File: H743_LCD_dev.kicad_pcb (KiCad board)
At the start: 6 copper layers, 80 x 65 mm, 76 parts, among them J1 Micro_SD_Card_Det_Hirose_DM3AT, J2 TFT_LCD, J3 CAPACITIVE_CONTROLLER, J4 USB-C, J5 I2C-STEMMA-QT, J7 Conn_02x05_Odd_Even, J8 SPKR, J9 UART, U1 W25Q128JVS, U2 IS42S16160J-7TL, U3 MT9284, U4 STM32H723ZGTx, U5 W25N01GVZEIG, U6 MAX98357AETE_, U7 CAT24C128, Y1 25MHz, Y2 32.768KHz

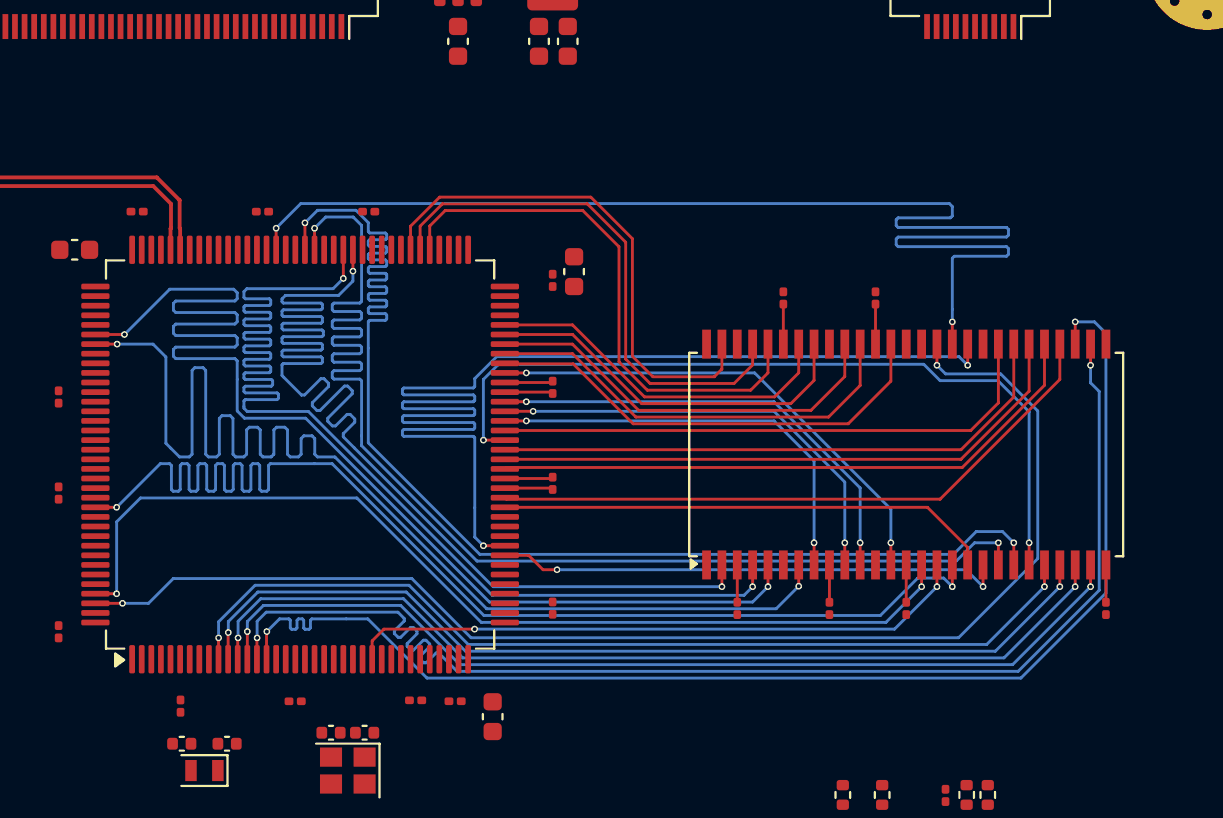
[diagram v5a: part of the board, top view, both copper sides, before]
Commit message: Finish high speed sdram tracks
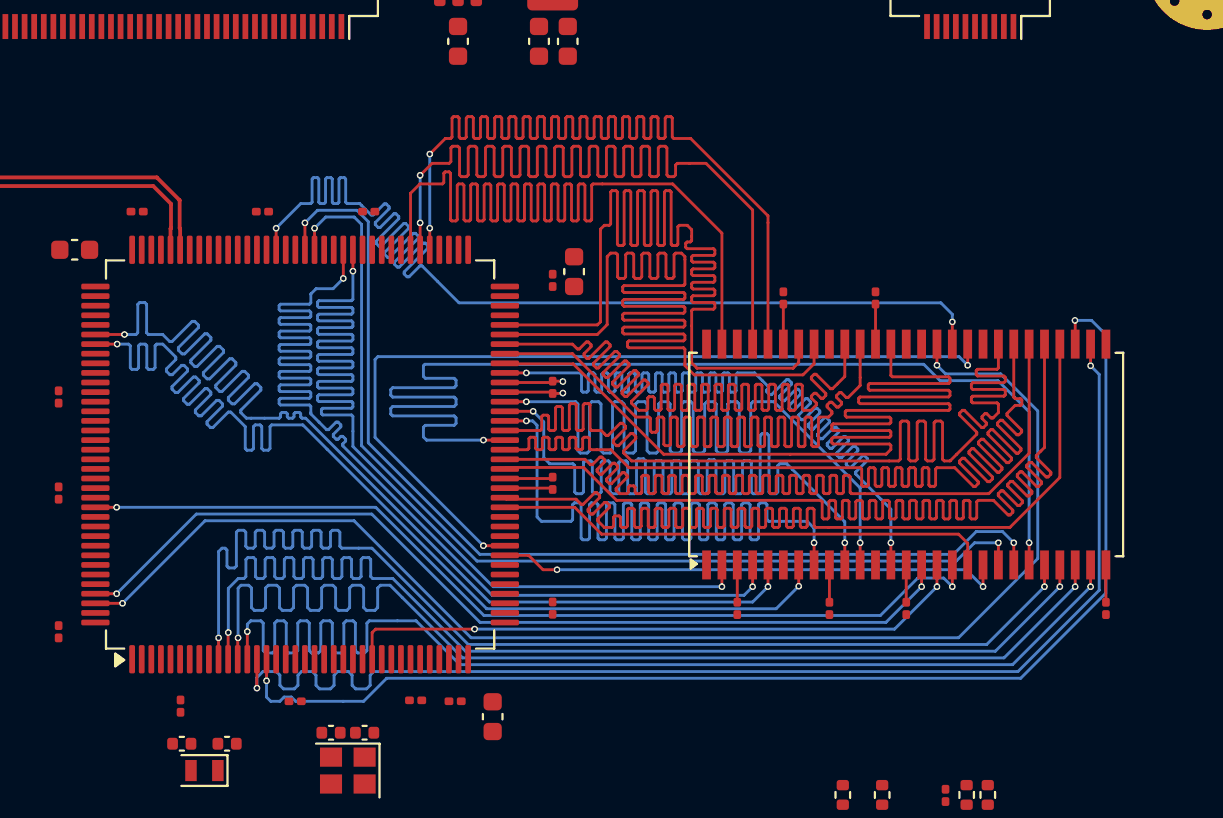
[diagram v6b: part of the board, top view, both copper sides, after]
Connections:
- net /MCU/A0 renamed /MCU/SDRAM_ADD0
- net /MCU/A1 renamed /MCU/SDRAM_ADD1
- net /MCU/A10 renamed /MCU/SDRAM_ADD10
- net /MCU/A11 renamed /MCU/SDRAM_ADD11
- net /MCU/A2 renamed /MCU/SDRAM_ADD2
- net /MCU/A3 renamed /MCU/SDRAM_ADD3
- net /MCU/A4 renamed /MCU/SDRAM_ADD4
- net /MCU/A5 renamed /MCU/SDRAM_ADD5
- net /MCU/A6 renamed /MCU/SDRAM_ADD6
- net /MCU/A7 renamed /MCU/SDRAM_ADD7
- net /MCU/A8 renamed /MCU/SDRAM_ADD8
- net /MCU/A9 renamed /MCU/SDRAM_ADD9
- net /MCU/DQ0 renamed /MCU/SDRAM_DQ0
- net /MCU/DQ1 renamed /MCU/SDRAM_DQ1
- net /MCU/DQ10 renamed /MCU/SDRAM_DQ10
- net /MCU/DQ11 renamed /MCU/SDRAM_DQ11
- net /MCU/DQ12 renamed /MCU/SDRAM_DQ12
- net /MCU/DQ13 renamed /MCU/SDRAM_DQ13
- net /MCU/DQ14 renamed /MCU/SDRAM_DQ14
- net /MCU/DQ15 renamed /MCU/SDRAM_DQ15
- net /MCU/DQ2 renamed /MCU/SDRAM_DQ2
- net /MCU/DQ3 renamed /MCU/SDRAM_DQ3
- net /MCU/DQ4 renamed /MCU/SDRAM_DQ4
- net /MCU/DQ5 renamed /MCU/SDRAM_DQ5
- net /MCU/DQ6 renamed /MCU/SDRAM_DQ6
- net /MCU/DQ7 renamed /MCU/SDRAM_DQ7
- net /MCU/DQ8 renamed /MCU/SDRAM_DQ8
- net /MCU/DQ9 renamed /MCU/SDRAM_DQ9
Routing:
- net /MCU/SDRAM_DQ12: track 18.9 -> 68.0 mm
- net /MCU/SDRAM_DQ11: track 20.0 -> 68.0 mm
- net /MCU/SDRAM_DQ10: track 21.5 -> 68.0 mm
- net /MCU/SDRAM_DQ8: track 24.3 -> 68.0 mm
- net /MCU/SDRAM_DQ4: track 22.4 -> 64.9 mm
- net /MCU/SDRAM_DQ5: track 23.5 -> 64.9 mm
- net /MCU/SDRAM_DQ15: track 27.0 -> 68.0 mm
- net /MCU/SDRAM_DQ6: track 24.4 -> 64.9 mm
- net /MCU/SDRAM_DQ14: track 28.0 -> 67.9 mm, vias 0 -> 2
- net /MCU/SDRAM_DQ7: track 25.9 -> 64.9 mm
- net /MCU/SDRAM_ADD11: track 29.4 -> 68.0 mm
- net /MCU/SDRAM_DQ9: track 22.7 -> 60.7 mm
- net /MCU/SDRAM_ADD9: track 30.4 -> 68.0 mm
- net /MCU/SDRAM_ADD8: track 31.2 -> 68.0 mm
- net /MCU/SDRAM_DQ13: track 28.4 -> 64.9 mm, vias 0 -> 2
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
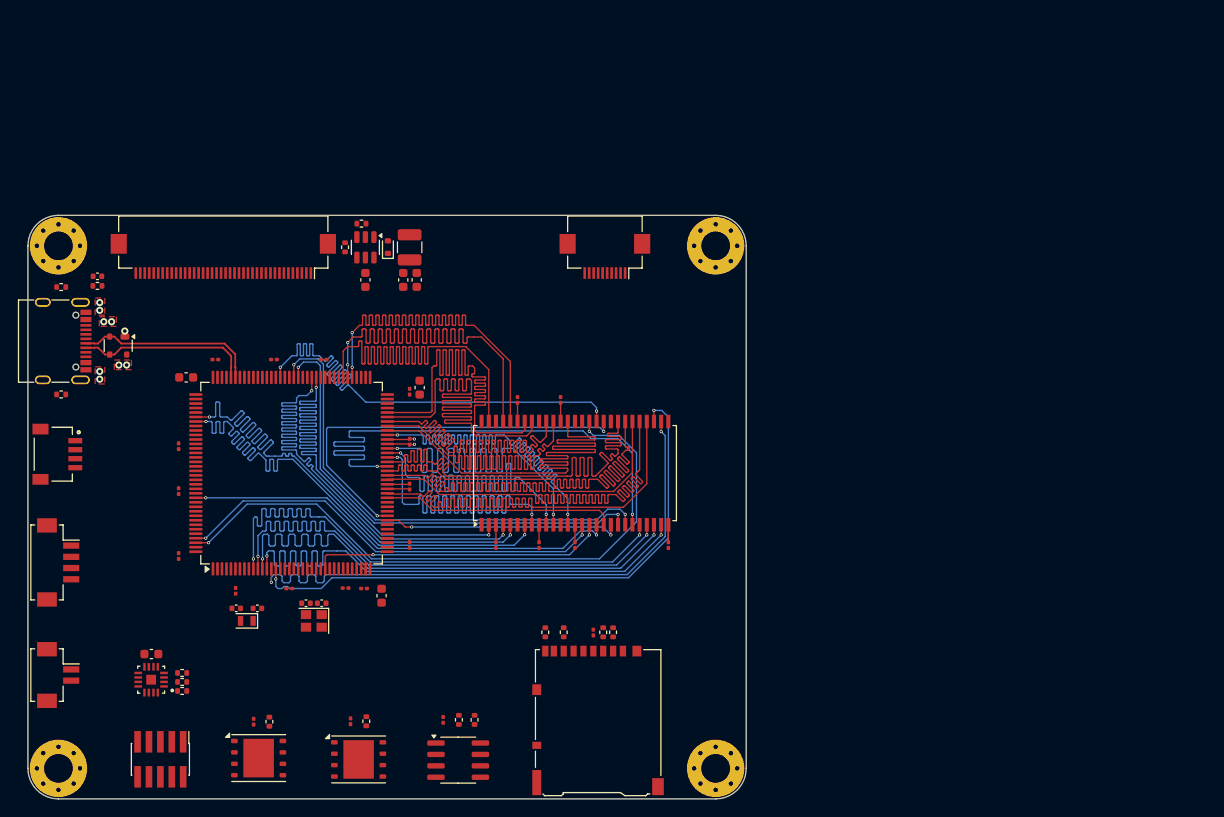
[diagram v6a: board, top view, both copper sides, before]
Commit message: Finish sdram, LCD, SD-card, QSPI, I2S tracks
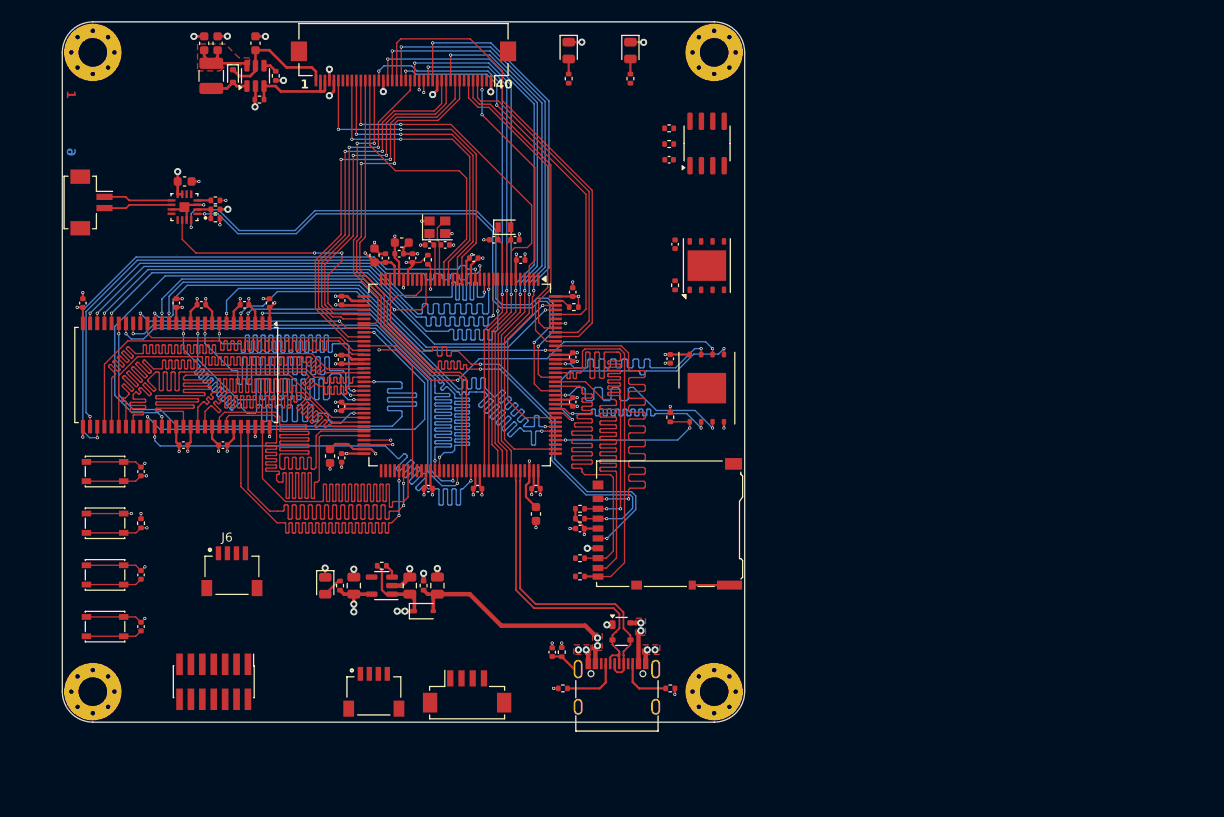
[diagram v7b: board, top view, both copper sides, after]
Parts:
- removed J7: Conn_02x05_Odd_Even, Connector_PinHeader_1.27mm:PinHeader_2x05_P1.27mm_Vertical_SMD
- added C24: 100n, Capacitor_SMD:C_0402_1005Metric, F.Cu at (115.0, 98.4)
- added C25: 100n, Capacitor_SMD:C_0402_1005Metric, F.Cu at (143.7, 74.2)
- added C26: 1u, Capacitor_SMD:C_0603_1608Metric, F.Cu at (144.0, 72.9)
- added C27: 100n, Capacitor_SMD:C_0402_1005Metric, F.Cu at (115.0, 109.9)
- added C28: 100n, Capacitor_SMD:C_0402_1005Metric, F.Cu at (115.0, 115.7)
- added C29: 100n, Capacitor_SMD:C_0402_1005Metric, F.Cu at (129.3, 79.7)
- added C30: 1u, Capacitor_SMD:C_0805_2012Metric, F.Cu at (144.9, 111.1)
- added C44: 2.2u, Capacitor_SMD:C_0805_2012Metric, F.Cu at (138.7, 111.1)
- added C45: 10u, Capacitor_SMD:C_0805_2012Metric, F.Cu at (148.0, 111.1)
- added D3: NSR0340HT1G, Diode_SMD:D_SOD-323, F.Cu at (146.5, 114.0)
- added D4: LED, LED_SMD:LED_0805_2012Metric, F.Cu at (135.5, 111.2)
- added D5: LED, LED_SMD:LED_0805_2012Metric, F.Cu at (169.5, 51.5)
- added D6: LED, LED_SMD:LED_0805_2012Metric, F.Cu at (162.6, 51.5)
- added J6: UART, SM04B-SRSS-TB_LF__SN_:JST_SM04B-SRSS-TB_LF__SN_, F.Cu at (125.1, 107.5)
- added R17: 10K, Resistor_SMD:R_0402_1005Metric, F.Cu at (146.9, 74.8)
- added R18: 10K, Resistor_SMD:R_0402_1005Metric, F.Cu at (115.0, 104.2)
- added R19: 10K, Resistor_SMD:R_0402_1005Metric, F.Cu at (163.2, 80.1)
- added R20: 10K, Resistor_SMD:R_0402_1005Metric, F.Cu at (141.8, 108.9)
- added R21: 2K2, Resistor_SMD:R_0402_1005Metric, F.Cu at (137.1, 111.1)
- added R22: 100K, Resistor_SMD:R_0402_1005Metric, F.Cu at (146.4, 111.1)
- added R23: 1K, Resistor_SMD:R_0402_1005Metric, F.Cu at (169.5, 54.7)
- added R24: 1K, Resistor_SMD:R_0402_1005Metric, F.Cu at (162.6, 54.7)
- added SW1: SW_Push, Button_Switch_SMD:SW_SPST_PTS810, F.Cu at (111.0, 98.4)
- added SW2: SW_Push, Button_Switch_SMD:SW_SPST_PTS810, F.Cu at (111.0, 104.2)
- added SW3: SW_Push, Button_Switch_SMD:SW_SPST_PTS810, F.Cu at (111.0, 109.9)
- added SW4: SW_Push, Button_Switch_SMD:SW_SPST_PTS810, F.Cu at (111.0, 115.7)
- added U8: TLV75733PDBV, Package_TO_SOT_SMD:SOT-23-5, F.Cu at (141.8, 111.1)
- C1, C10, C11, C12, C13, C14, C15, C16, C17, C18, C2, C20, C21, C22, C3, C36, C37, C38, C4, C5, C6, C7, C8, C9: footprint Capacitor_SMD:C_0201_0603Metric -> Capacitor_SMD:C_0402_1005Metric
- J3: value CAPACITIVE_CONTROLLER -> swd; footprint Connector_FFC-FPC:Hirose_FH12-10S-0.5SH_1x10-1MP_P0.50mm_Horizontal -> Connector_PinHeader_1.27mm:PinHeader_2x07_P1.27mm_Vertical_SMD
- U1: footprint Package_SON:WSON-8-1EP_6x5mm_P1.27mm_EP3.4x4.3mm -> Package_SON:WSON-8-1EP_8x6mm_P1.27mm_EP3.4x4.3mm
- moved H2 108.1 mm to (178.8, 51.7), turned to 180 degrees
- moved H1 105.7 mm to (109.6, 51.7), turned to 180 degrees
- moved H3 88.3 mm to (178.8, 122.9), turned to 180 degrees
- moved H4 85.3 mm to (109.6, 122.9), turned to 180 degrees
- moved R12 75.3 mm to (173.9, 122.6)
- moved J4 74.3 mm to (168.0, 123.6), turned to 0 degrees
- moved U7 74.1 mm to (178.0, 61.9), turned to 90 degrees
- moved R11 71.6 mm to (162.0, 122.6), turned to 0 degrees
- moved C1 70.6 mm to (108.5, 79.7), turned to 90 degrees
- moved R6 69.4 mm to (173.8, 60.2), turned to 180 degrees
- moved R5 68.3 mm to (173.8, 61.9), turned to 180 degrees
- moved U5 67.3 mm to (178.0, 75.5), turned to 90 degrees
- moved C20 67.3 mm to (173.8, 63.7), turned to 180 degrees
- moved R13 65.9 mm to (161.8, 118.5), turned to 90 degrees
- moved C43 65.7 mm to (160.8, 118.5), turned to 90 degrees
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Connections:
- C32 pad 1: Net-(U3-VIN) -> VDD
- C33 pad 1: Net-(U3-VIN) -> VDD
- J1 pad 1: /MEMORY/SD_DAT2 -> /MCU/SD_DAT2
- J1 pad 2: /MEMORY/SD_DAT3/CD -> /MCU/SD_DAT3
- J1 pad 3: /MEMORY/SD_CMD -> /MCU/SD_CMD
- J1 pad 5: /MEMORY/SD_CLK -> /MCU/SD_CLK
- J1 pad 7: /MEMORY/SD_DAT0 -> /MCU/SD_DAT0
- J1 pad 8: /MEMORY/SD_DAT1 -> /MCU/SD_DAT1
- J1 pad 9: /MEMORY/SD_DET -> /MCU/PG13
- J2 pad 1: /LCD/LED_K -> GND
- J2 pad 11: /LCD/LCD_R6 -> /LCD/LCD_R4
- J2 pad 12: /LCD/LCD_R7 -> /LCD/LCD_R3
- J2 pad 13: /LCD/LCD_G0 -> GND
- J2 pad 14: /LCD/LCD_G1 -> /LCD/LCD_G7
- J2 pad 15: /LCD/LCD_G2 -> /LCD/LCD_G6
- J2 pad 16: /LCD/LCD_G3 -> /LCD/LCD_G5
- J2 pad 18: /LCD/LCD_G5 -> /LCD/LCD_G3
- J2 pad 19: /LCD/LCD_G6 -> /LCD/LCD_G2
- J2 pad 2: /LCD/LED_A -> +3V3
- J2 pad 20: /LCD/LCD_G7 -> /LCD/LCD_B7
- J2 pad 21: /LCD/LCD_B0 -> /LCD/LCD_B6
- J2 pad 22: /LCD/LCD_B1 -> /LCD/LCD_B5
- J2 pad 23: /LCD/LCD_B2 -> /LCD/LCD_B4
- J2 pad 25: /LCD/LCD_B4 -> GND
- J2 pad 26: /LCD/LCD_B5 -> /LCD/HSYNC
- J2 pad 27: /LCD/LCD_B6 -> /LCD/VSYNC
- J2 pad 28: /LCD/LCD_B7 -> /LCD/LCD_DE
- J2 pad 29: GND -> /LCD/LCD_CLK
- J2 pad 3: unconnected-(J2-Pad3) -> /LCD/LCD_TP_RST
- J2 pad 30: /LCD/LCD_CLK -> /LCD/LCD_SPI_CS
- J2 pad 31: /LCD/LCD_DISP -> /LCD/LCD_SPI_CLK
- J2 pad 32: /LCD/HSYNC -> /LCD/LCD_SPI_DAT
- J2 pad 33: /LCD/VSYNC -> unconnected-(J2-Pad33)
- J2 pad 34: /LCD/LCD_DE -> unconnected-(J2-Pad34)
- J2 pad 35: unconnected-(J2-Pad35) -> /LCD/LCD_RESET
- J2 pad 36: GND -> +3V3
- J2 pad 37: /LCD/XR -> GND
- J2 pad 38: /LCD/YD -> /LCD/LED_K
- J2 pad 39: /LCD/XL -> /LCD/LED_K
- J2 pad 4: VDD -> /LCD/LCD_TP_SCL
- J2 pad 40: /LCD/YU -> /LCD/LED_A
- J2 pad 5: /LCD/LCD_R0 -> /LCD/LCD_TP_SDA
- J2 pad 6: /LCD/LCD_R1 -> /LCD/LCD_TP_INT
- J2 pad 7: /LCD/LCD_R2 -> GND
- J2 pad 8: /LCD/LCD_R3 -> /LCD/LCD_R7
- J2 pad 9: /LCD/LCD_R4 -> /LCD/LCD_R6
- J3 pad 1: GND -> unconnected-(J3-Pin_1-Pad1)
- J3 pad 10: GND -> unconnected-(J3-Pin_10-Pad10)
- J3 pad 2: VDD -> unconnected-(J3-Pin_2-Pad2)
- J3 pad 3: /LCD/LCD_SCL -> unconnected-(J3-Pin_3-Pad3)
- J3 pad 4: GND -> unconnected-(J3-Pin_4-Pad4)
- J3 pad 5: /LCD/LCD_SDA -> unconnected-(J3-Pin_5-Pad5)
- J3 pad 6: GND -> unconnected-(J3-Pin_6-Pad6)
- J3 pad 7: /LCD/~{LCD_RST} -> unconnected-(J3-Pin_7-Pad7)
- J3 pad 8: /LCD/LCD_WAKE -> unconnected-(J3-Pin_8-Pad8)
- J3 pad 9: /LCD/~{LCD_INT} -> unconnected-(J3-Pin_9-Pad9)
- L1 pad 1: Net-(U3-VIN) -> VDD
- R10 pad 1: /MEMORY/SD_DET -> /MCU/PG13
- R14 pad 1: /Audio/I2S_SD_MODE -> /MCU/I2S_SD_MODE
- R2 pad 2: /MEMORY/~{NOR_CS} -> /MCU/~{NOR_CS}
- R7 pad 2: /MEMORY/SD_DAT0 -> /MCU/SD_DAT0
- R8 pad 2: /MEMORY/SD_CMD -> /MCU/SD_CMD
- R9 pad 2: /MEMORY/SD_DAT3/CD -> /MCU/SD_DAT3
- U1 pad 1: /MEMORY/~{NOR_CS} -> /MCU/~{NOR_CS}
- U1 pad 2: /MEMORY/NOR_DO(IO1) -> /MCU/NOR_D1
- U1 pad 3: /MEMORY/NOR_IO2 -> /MCU/NOR_D2
- U1 pad 5: /MEMORY/NOR_DI(IO0) -> /MCU/NOR_D0
- U1 pad 6: /MEMORY/NOR_CLK -> /MCU/NOR_CLK
- U1 pad 7: /MEMORY/NOR_IO3 -> /MCU/NOR_D3
- U3 pad 6: Net-(U3-VIN) -> VDD
- U4 pad 100: /MCU/PA8 -> /LCD/LCD_B3
- U4 pad 101: /MCU/PA9 -> /LCD/LCD_R5
- U4 pad 102: /MCU/PA10 -> /LCD/LCD_B4
- U4 pad 110: /MCU/PA15(JTDI) -> /LCD/LCD_B6
- U4 pad 112: /MCU/PC11 -> /MCU/~{NOR_CS}
- U4 pad 117: /MCU/PD3 -> /LCD/LCD_G7
- U4 pad 118: /MCU/PD4 -> /MCU/NOR_D0
- U4 pad 119: /MCU/PD5 -> /MCU/NOR_D1
- U4 pad 122: /MCU/PD6 -> /MCU/NOR_D2
- U4 pad 123: /MCU/PD7 -> /MCU/I2S_SDO
- U4 pad 124: /MCU/PG9 -> /MCU/SD_DAT0
- U4 pad 125: /MCU/PG10 -> /MCU/SD_DAT1
- U4 pad 126: /MCU/PG11 -> /MCU/I2S_CK
- U4 pad 127: /MCU/PG12 -> /MCU/SD_DAT3
- U4 pad 129: /MCU/PG14 -> /MCU/NOR_D3
- U4 pad 133: /MCU/PB3(JTDO -> /MCU/SD_DAT2
- U4 pad 134: /MCU/PB4(NJTRST) -> /LCD/LCD_TP_INT
- U4 pad 135: /MCU/PB5 -> /LCD/LCD_B5
- U4 pad 136: /MCU/PB6 -> /LCD/LCD_TP_SCL
- U4 pad 137: /MCU/PB7 -> /LCD/LCD_TP_SDA
- U4 pad 140: /MCU/PB9 -> /LCD/LCD_B7
- U4 pad 143: unconnected-(U4-PDR_ON-Pad143) -> Net-(U4-PDR_ON)
- U4 pad 18: /MCU/PF6 -> /LCD/LCD_RESET
- U4 pad 19: /MCU/PF7 -> /LCD/LCD_SPI_CLK
- U4 pad 21: /MCU/PF9 -> /LCD/LCD_SPI_DAT
- U4 pad 22: /MCU/PF10 -> /LCD/LCD_DE
- U4 pad 25: unconnected-(U4-NRST-Pad25) -> /MCU/NRST
- U4 pad 27: /MCU/PC1 -> /MCU/SD_CLK
- U4 pad 3: /MCU/PE4 -> /LCD/LCD_TP_RST
- U4 pad 32: unconnected-(U4-VREF+-Pad32) -> +3V3
- U4 pad 34: /MCU/PA0 -> /MCU/SD_CMD
- U4 pad 40: /MCU/PA4 -> /MCU/I2S_WS
- U4 pad 41: /MCU/PA5 -> /LCD/LCD_R4
- U4 pad 42: /MCU/PA6 -> /LCD/LCD_G2
- U4 pad 43: /MCU/PA7 -> /LCD/VSYNC
- U4 pad 46: /MCU/PB0 -> /LCD/LCD_R3
- U4 pad 47: /MCU/PB1 -> /LCD/LCD_R6
- U4 pad 48: /MCU/PB2 -> /MCU/NOR_CLK
- U4 pad 69: /MCU/PB10 -> /LCD/LCD_G4
- U4 pad 7: /MCU/PC13 -> /LCD/LCD_SPI_CS
- U4 pad 70: /MCU/PB11 -> /LCD/LCD_G5
- U4 pad 80: /MCU/PD11 -> /MCU/I2S_SD_MODE
- U4 pad 91: /MCU/PG6 -> /LCD/LCD_R7
- U4 pad 92: /MCU/PG7 -> /LCD/LCD_CLK
- U4 pad 96: /MCU/PC6 -> /LCD/HSYNC
- U4 pad 97: /MCU/PC7 -> /LCD/LCD_G6
- U4 pad 99: /MCU/PC9 -> /LCD/LCD_G3
- U6 pad 1: /Audio/I2S_SDO -> /MCU/I2S_SDO
- U6 pad 14: /Audio/I2S_WS -> /MCU/I2S_WS
- U6 pad 16: /Audio/I2S_CK -> /MCU/I2S_CK
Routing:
- net GND: track 5.58 -> 120.6 mm, vias 6 -> 69
- net /MCU/BOOT0: track 0.00 -> 73.3 mm, vias 0 -> 2
- net +3V3: track 17.5 -> 90.6 mm, vias 1 -> 29
- net /LCD/LCD_B6: track 0.00 -> 67.9 mm, vias 0 -> 2
- net /LCD/LCD_B4: track 0.00 -> 65.7 mm, vias 0 -> 2
- net /MCU/I2S_CK: track 0.00 -> 64.6 mm, vias 0 -> 2
- net /LCD/LCD_B3: track 0.00 -> 63.8 mm, vias 0 -> 2
- net /MCU/I2S_SDO: track 0.00 -> 62.6 mm, vias 0 -> 2
- net /LCD/LCD_G7: track 0.00 -> 61.2 mm, vias 0 -> 2
- net /MCU/SD_DAT0: track 0.00 -> 60.5 mm
- net /MCU/SD_DAT3: track 0.00 -> 59.9 mm, vias 0 -> 2
- net /LCD/LCD_R7: track 0.00 -> 59.7 mm, vias 0 -> 2
- net /LCD/HSYNC: track 0.00 -> 59.7 mm, vias 0 -> 2
- net /MCU/NRST: track 0.00 -> 59.3 mm, vias 0 -> 2
- net /MCU/SD_DAT1: track 0.00 -> 59.0 mm
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- added copper zone on In2.Cu, net +3V3
- added copper zone on In2.Cu, net VBUS
- added copper zone on F.Cu, net VDD
- added copper zone on In3.Cu, net VDD
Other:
- board size 80 x 65 mm -> 76 x 78 mm
- board text added: "1"
- board text added: "2"
- board text added: "3"
- board text added: "4"
- board text added: "40"
- board text added: "5"
- board text added: "6"

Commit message: Looks like FPC should be changed to XF2M-4015-1A
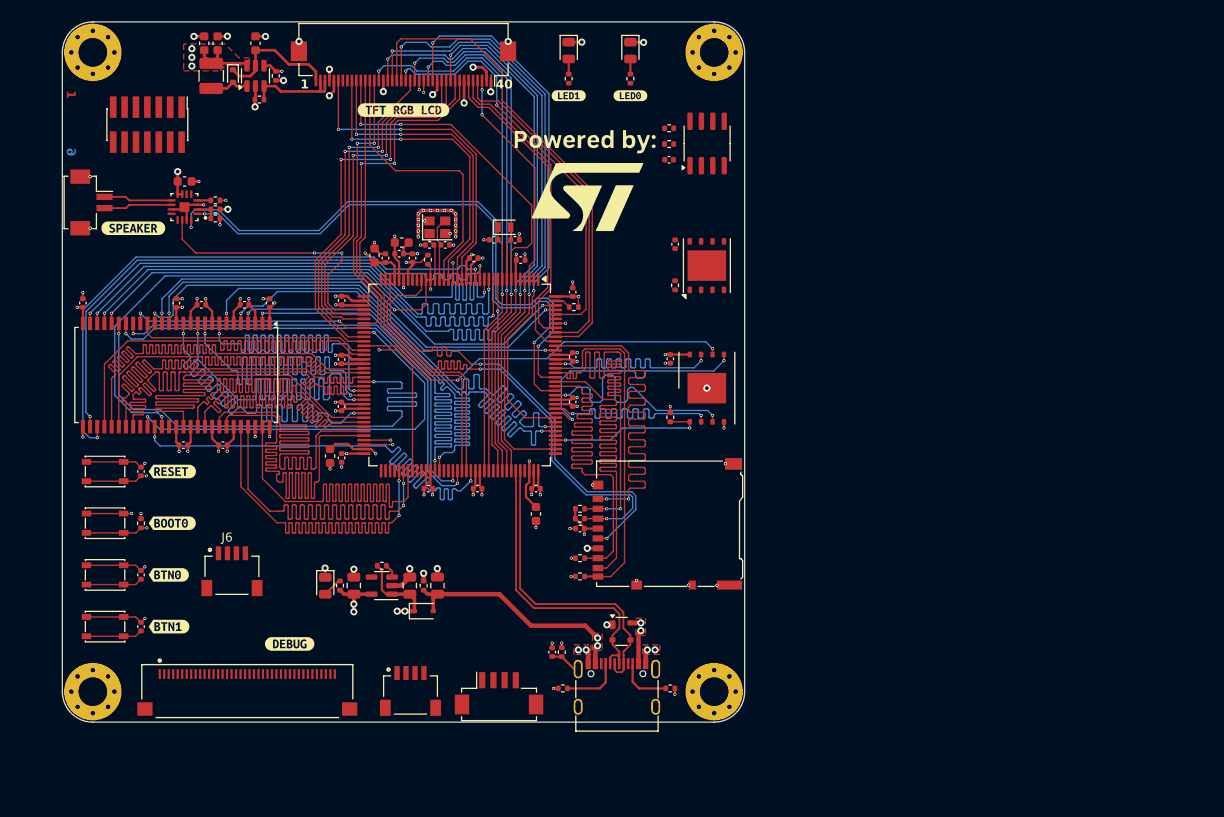
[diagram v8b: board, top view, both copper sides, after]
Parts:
- added G***: LOGO, powered_by_st:powered_by_st_25x25, F.Cu at (164.4, 67.8)
- added G***: LOGO, powered_by_st:powered_by_st, B.Cu at (144.3, 91.0)
- added J7: ~, FPC-40P-Omron-XF2M-4015-1Apretty:Omron-XF2M-4015-1A-R100-0-0-0, F.Cu at (126.8, 122.9)
- added kibuzzard-66417165: G***, kibuzzard-66417165, F.Cu at (131.5, 117.6)
- added kibuzzard-66417197: G***, kibuzzard-66417197, F.Cu at (144.2, 58.2)
- added kibuzzard-66418113: G***, kibuzzard-66418113, F.Cu at (114.1, 71.3)
- added kibuzzard-6641818D: G***, kibuzzard-6641818D, F.Cu at (169.5, 56.6)
- added kibuzzard-66418194: G***, kibuzzard-66418194, F.Cu at (162.6, 56.6)
- added kibuzzard-6641D19D: G***, kibuzzard-6641D19D, F.Cu at (118.4, 98.4)
- added kibuzzard-6641D1A5: G***, kibuzzard-6641D1A5, F.Cu at (118.4, 104.2)
- added kibuzzard-6641D1AA: G***, kibuzzard-6641D1AA, F.Cu at (118.1, 109.9)
- added kibuzzard-6641D1B0: G***, kibuzzard-6641D1B0, F.Cu at (118.1, 115.7)
- C39, C40: value 10p -> 16p
- C41, C42: value 22p -> 10p
- D3: value NSR0340HT1G -> NSR0320MW2T1G
- D4: value LED -> GREEN
- D5, D6: value LED -> RED
- moved J3 62.5 mm to (115.7, 59.8)
- moved J5 4.08 mm to (145.0, 120.9)
- moved J9 3.56 mm to (154.8, 123.1)
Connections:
- U4 pad 20: /MCU/PF8 -> /LCD/LCD_BLK
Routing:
- net /LCD/LCD_BLK: track 1.57 -> 43.4 mm, vias 0 -> 2
- net GND: track 120.6 -> 136.2 mm, vias 69 -> 95
- net +3V3: track 90.6 -> 94.2 mm, vias 29 -> 32
- net /LCD/LCD_G6: track 54.8 -> 56.8 mm
- net /LCD/LCD_B7: track 44.6 -> 46.5 mm
- net /LCD/LCD_G3: track 57.8 -> 59.7 mm
- net /LCD/LCD_B3: track 63.8 -> 65.6 mm
- net /LCD/HSYNC: track 59.7 -> 61.4 mm
- net /LCD/LCD_B6: track 67.9 -> 69.5 mm
- net /MCU/I2S_SDO: track 62.6 -> 64.1 mm
- net /MCU/I2S_CK: track 64.6 -> 66.2 mm
- net /LCD/LCD_R5: track 57.9 -> 59.2 mm
- net /LCD/LCD_B4: track 65.7 -> 66.9 mm
- net /LCD/LCD_G7: track 61.2 -> 62.3 mm
- net VDD: vias 4 -> 7
